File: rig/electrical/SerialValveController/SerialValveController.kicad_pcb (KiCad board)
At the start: 2 copper layers, 72.2 x 50.8 mm, 21 parts, among them J1 Screw_Terminal_01x02, J17 Conn_01x05_Socket, J18 TST-105-01-X-D, J19 TST-105-01-X-D, J2 Screw_Terminal_01x02, U1 TPIC6595

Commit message: Serial Olfactometer improved design
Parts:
- moved C3 9.73 mm to (86.5, 78.9)
- moved CR2 9.73 mm to (126.1, 60.2)
- moved CR1 9.73 mm to (125.6, 71.4)
- moved H1 9.73 mm to (129.6, 82.3)
- moved C4 9.73 mm to (93.6, 77.9)
- moved D1 9.73 mm to (126.3, 66.3)
- moved D2 9.73 mm to (126.5, 54.9)
- moved H2 9.73 mm to (78.8, 82.3)
- moved J19 9.73 mm to (82.2, 73.2)
- moved R3 9.73 mm to (85.0, 50.8)
- moved R5 9.73 mm to (79.7, 50.8)
- moved C2 9.73 mm to (109.2, 74.2)
- moved J1 9.73 mm to (112.9, 74.5)
- moved J17 9.73 mm to (77.1, 45.7)
- moved J18 9.73 mm to (82.3, 58.9)
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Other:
- board text added: "(Fast Response)"
- board text added: "+24V"
- board text added: "0.1μF"
- board text added: "33Ω"
- board text added: "GND"

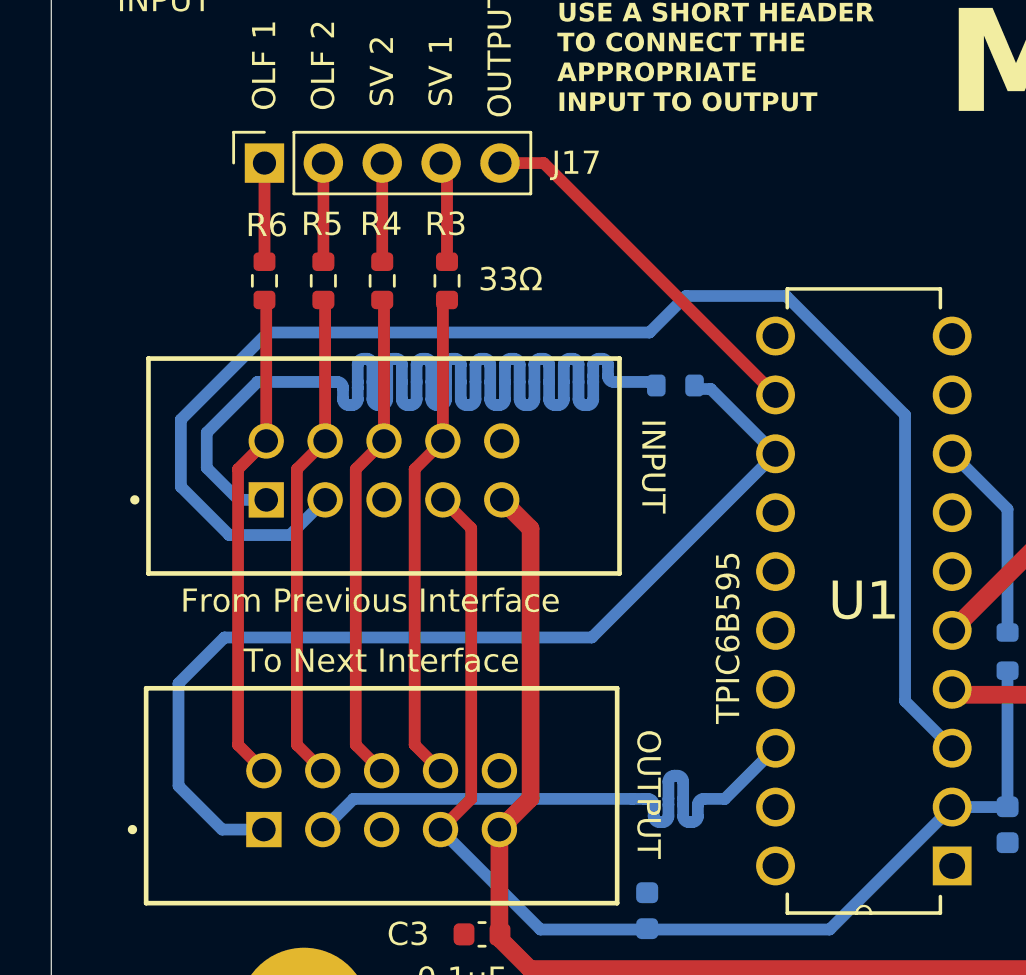
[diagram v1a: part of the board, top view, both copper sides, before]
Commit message: valve updated
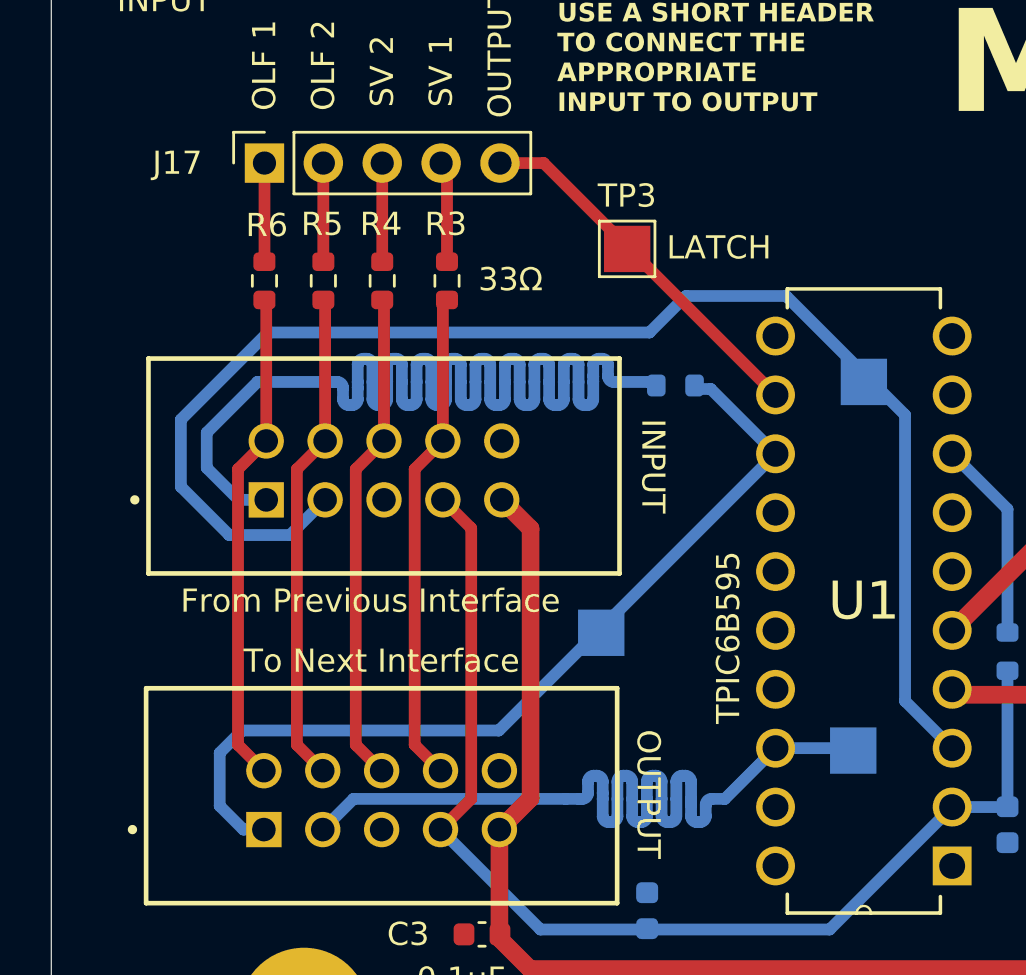
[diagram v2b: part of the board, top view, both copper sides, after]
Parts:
- added TP1: TestPoint, TestPoint:TestPoint_Pad_2.0x2.0mm, B.Cu at (103.0, 55.1)
- added TP2: TestPoint, TestPoint:TestPoint_Pad_2.0x2.0mm, B.Cu at (91.6, 65.9)
- added TP3: TestPoint, TestPoint:TestPoint_Pad_2.0x2.0mm, F.Cu at (92.8, 49.4)
- added TP4: TestPoint, TestPoint:TestPoint_Pad_2.0x2.0mm, B.Cu at (102.5, 71.0)
- R3, R4, R5, R6, R7: value R -> 33Ω
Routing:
- net Net-(U1-SER_OUT): track 26.0 -> 38.6 mm
- net Net-(U1-SRCK): track 43.4 -> 38.6 mm
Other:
- board text added: "10kΩ"
- board text added: "CLOCK IN"
- board text added: "CLOCK OUT"
- board text added: "LATCH"
- board text added: "SERIAL IN"
- board text added: "SERIAL OUT"

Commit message: Tweaking of v1 boards
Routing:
- net +5V: track 49.6 -> 57.6 mm
- net GND: vias 0 -> 3
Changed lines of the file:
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@@
 	)
 	(segment
-		(start 101.4984 78.74)
-		(end 106.7816 73.4568)
+		(start 84.709 74.4281)
+		(end 89.0209 78.74)
+		(width 0.508)
+		(layer "B.Cu")
+		(net 1)
+	)
+	(segment
+		(start 110.3438 73.4438)
+		(end 109.1692 73.4438)
 		(width 0.508)
 		(layer "B.Cu")
@@
 	)
 	(segment
-		(start 84.709 74.4281)
-		(end 89.0209 78.74)
+		(start 109.86 78.74)
+		(end 110.9 77.7)
+		(width 0.508)
+		(layer "B.Cu")
+		(net 1)
+	)
+	(segment
+		(start 110.9 77.7)
+		(end 110.9 74)
+		(width 0.508)
+		(layer "B.Cu")
+		(net 1)
+	)
+	(segment
+		(start 110.9 74)
+		(end 110.3438 73.4438)
 		(width 0.508)
 		(layer "B.Cu")
@@
 	(segment
 		(start 89.0209 78.74)
-		(end 101.4984 78.74)
+		(end 109.86 78.74)
 		(width 0.508)
 		(layer "B.Cu")
@@
 		(net 1)
 	)
+	(via
+		(at 81.9 67.7)
+		(size 0.6)
+		(drill 0.35)
+		(layers "F.Cu" "B.Cu")
+		(free yes)
+		(net 2)
+	)
+	(via
+		(at 81.9 66.1)
+		(size 0.6)
+		(drill 0.35)
+		(layers "F.Cu" "B.Cu")
+		(free yes)
+		(net 2)
+	)
+	(via
+		(at 81.9 66.9)
+		(size 0.6)
+		(drill 0.35)
+		(layers "F.Cu" "B.Cu")
+		(free yes)
+		(net 2)
+	)
 	(segment
